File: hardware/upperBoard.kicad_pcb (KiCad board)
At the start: 2 copper layers, 23 parts, among them J1 Program interface, J2 Conn_02x10_Odd_Even, Q1 MMBT3904, Q2 MMBT3904, SW1 Reset, SW2 Prog, U1 ESP-12F, U2 A2982, U3 MCP23017_SO, U4 A2982

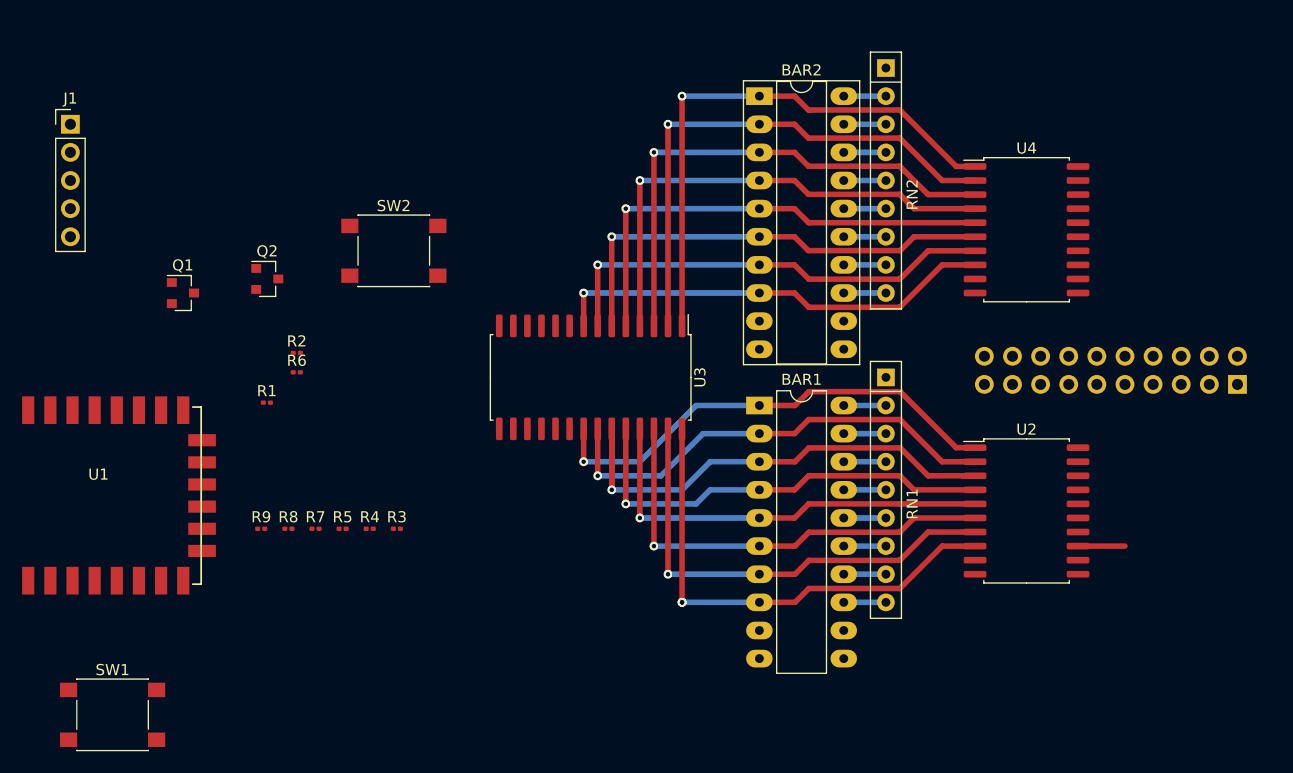
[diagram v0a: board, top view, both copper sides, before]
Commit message: move on to 16A relays
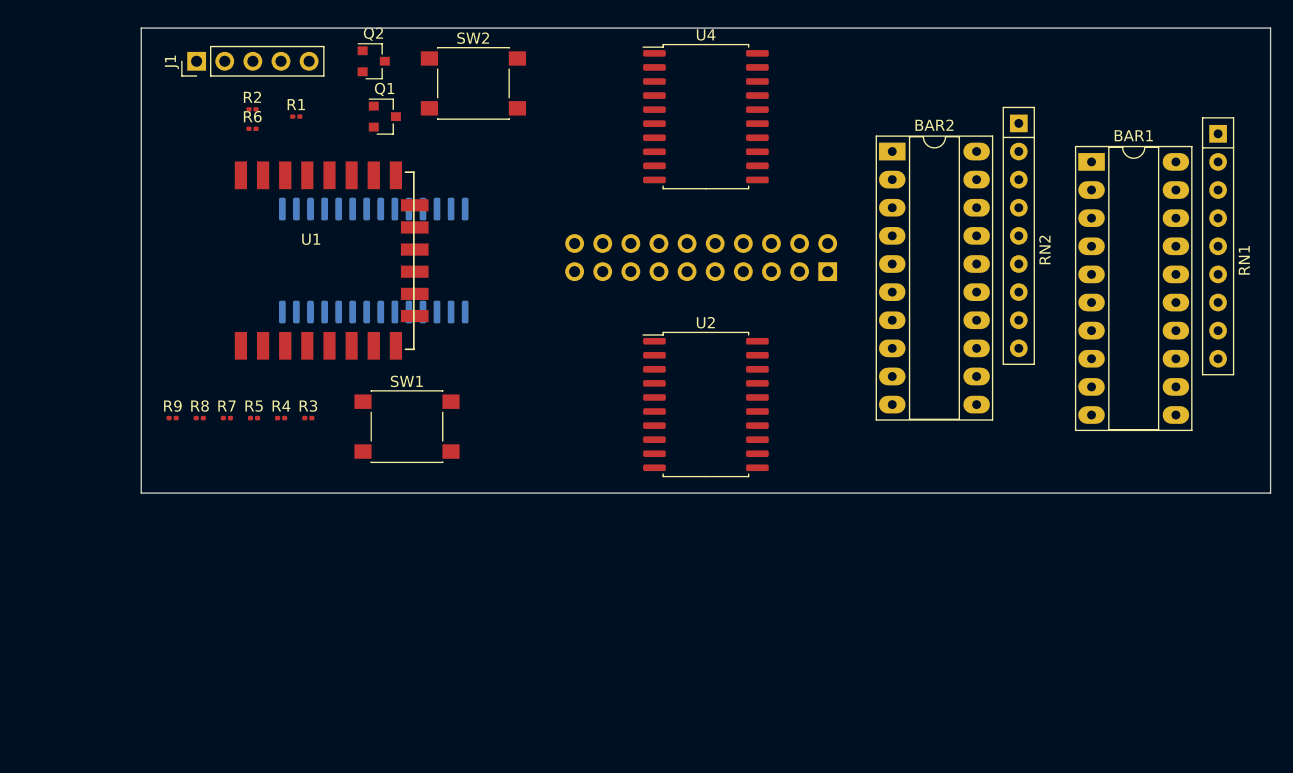
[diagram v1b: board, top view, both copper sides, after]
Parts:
- BAR1: footprint Package_DIP:DIP-20_W7.62mm_LongPads -> Package_DIP:DIP-20_W7.62mm_Socket_LongPads
- U3: moved to B.Cu
- moved J2 38.4 mm to (170.0, 73.0)
- moved SW1 37.2 mm to (132.0, 87.0)
- moved BAR1 37.2 mm to (193.8, 63.1)
- moved RN1 37.2 mm to (205.3, 60.5)
- moved U4 30.7 mm to (159.0, 59.0)
- moved U2 30.5 mm to (159.0, 85.0)
- moved U1 28.6 mm to (117.0, 79.0)
- moved R1 26.0 mm to (122.0, 59.0)
- moved Q1 24.2 mm to (130.0, 59.0)
- moved R2 22.4 mm to (118.0, 58.3)
- moved R6 22.4 mm to (118.0, 60.1)
- moved U3 22.3 mm to (129.0, 72.0), turned to 90 degrees
- moved Q2 21.9 mm to (129.0, 54.0)
- moved SW2 16.7 mm to (138.0, 56.0)
- moved BAR2 13.0 mm to (175.8, 62.1)
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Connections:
- BAR2 pad 10: Net-(BAR2-Pad10) -> (no net)
- BAR2 pad 11: Net-(BAR2-Pad11) -> (no net)
- BAR2 pad 12: Net-(BAR2-Pad12) -> (no net)
- BAR2 pad 9: Net-(BAR2-Pad9) -> (no net)
- J2 pad 1: /01 -> /08
- J2 pad 10: /10 -> /13
- J2 pad 11: /11 -> /03
- J2 pad 12: /12 -> /14
- J2 pad 13: /13 -> /02
- J2 pad 14: /14 -> /15
- J2 pad 15: /15 -> /01
- J2 pad 2: /02 -> /09
- J2 pad 3: /03 -> /07
- J2 pad 4: /04 -> /10
- J2 pad 5: /05 -> /06
- J2 pad 6: /06 -> /11
- J2 pad 7: /07 -> /05
- J2 pad 8: /08 -> /12
- J2 pad 9: /09 -> /04
- U1 pad 17: Net-(U1-Pad17) -> (no net)
- U1 pad 18: Net-(U1-Pad18) -> (no net)
- U1 pad 19: Net-(U1-Pad19) -> (no net)
- U1 pad 2: Net-(U1-Pad2) -> (no net)
- U1 pad 20: Net-(U1-Pad20) -> (no net)
- U1 pad 21: Net-(U1-Pad21) -> (no net)
- U1 pad 22: Net-(U1-Pad22) -> (no net)
- U1 pad 4: Net-(U1-Pad4) -> (no net)
- U1 pad 5: Net-(U1-Pad5) -> (no net)
- U1 pad 6: Net-(U1-Pad6) -> (no net)
- U1 pad 7: Net-(U1-Pad7) -> (no net)
- U2 pad 10: Net-(U2-Pad10) -> (no net)
- U2 pad 11: Net-(U2-Pad11) -> (no net)
- U3 pad 11: Net-(U3-Pad11) -> (no net)
- U3 pad 14: Net-(U3-Pad14) -> (no net)
- U3 pad 19: Net-(U3-Pad19) -> (no net)
- U3 pad 20: Net-(U3-Pad20) -> (no net)
- U4 pad 10: Net-(U4-Pad10) -> (no net)
- U4 pad 11: Net-(U4-Pad11) -> (no net)
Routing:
- net Net-(BAR2-Pad1): track 49.4 -> 0.00 mm, vias 1 -> 0
- net Net-(BAR1-Pad3): track 48.1 -> 0.00 mm, vias 1 -> 0
- net Net-(BAR2-Pad2): track 48.0 -> 0.00 mm, vias 1 -> 0
- net Net-(BAR2-Pad3): track 46.3 -> 0.00 mm, vias 1 -> 0
- net Net-(BAR2-Pad4): track 44.5 -> 0.00 mm, vias 1 -> 0
- net Net-(BAR1-Pad8): track 44.2 -> 0.00 mm, vias 2 -> 0
- net Net-(BAR1-Pad1): track 43.0 -> 0.00 mm, vias 1 -> 0
- net Net-(BAR2-Pad5): track 42.7 -> 0.00 mm, vias 1 -> 0
- net Net-(BAR1-Pad7): track 42.5 -> 0.00 mm, vias 1 -> 0
- net Net-(BAR1-Pad2): track 42.0 -> 0.00 mm, vias 1 -> 0
- net Net-(BAR2-Pad6): track 41.9 -> 0.00 mm, vias 1 -> 0
- net Net-(BAR2-Pad7): track 41.2 -> 0.00 mm, vias 1 -> 0
- net Net-(BAR1-Pad6): track 40.7 -> 0.00 mm, vias 1 -> 0
- net Net-(BAR2-Pad8): track 40.4 -> 0.00 mm, vias 1 -> 0
- net Net-(BAR1-Pad4): track 39.9 -> 0.00 mm, vias 1 -> 0
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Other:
- board outline added: 102 x 42 mm
